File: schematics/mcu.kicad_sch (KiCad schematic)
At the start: 7 parts, among them SW0 SW_SPST, U1 ESP32-C3-WROOM-02

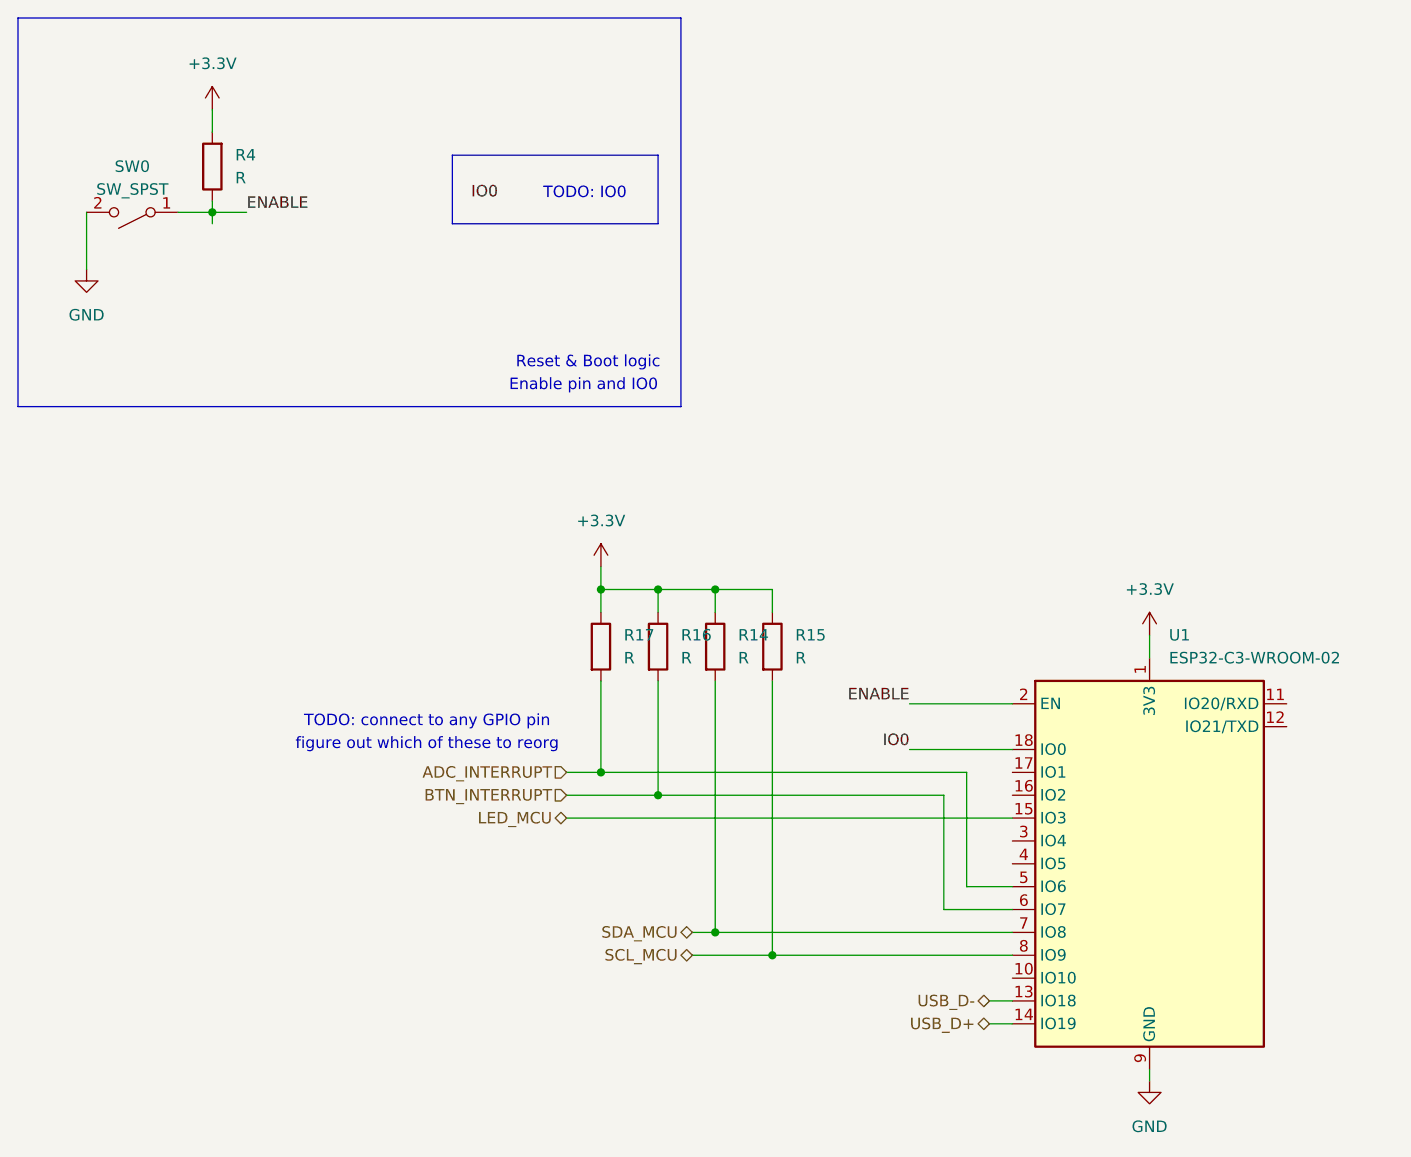
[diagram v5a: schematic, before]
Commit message: Fix layout, rewiring, and clearances
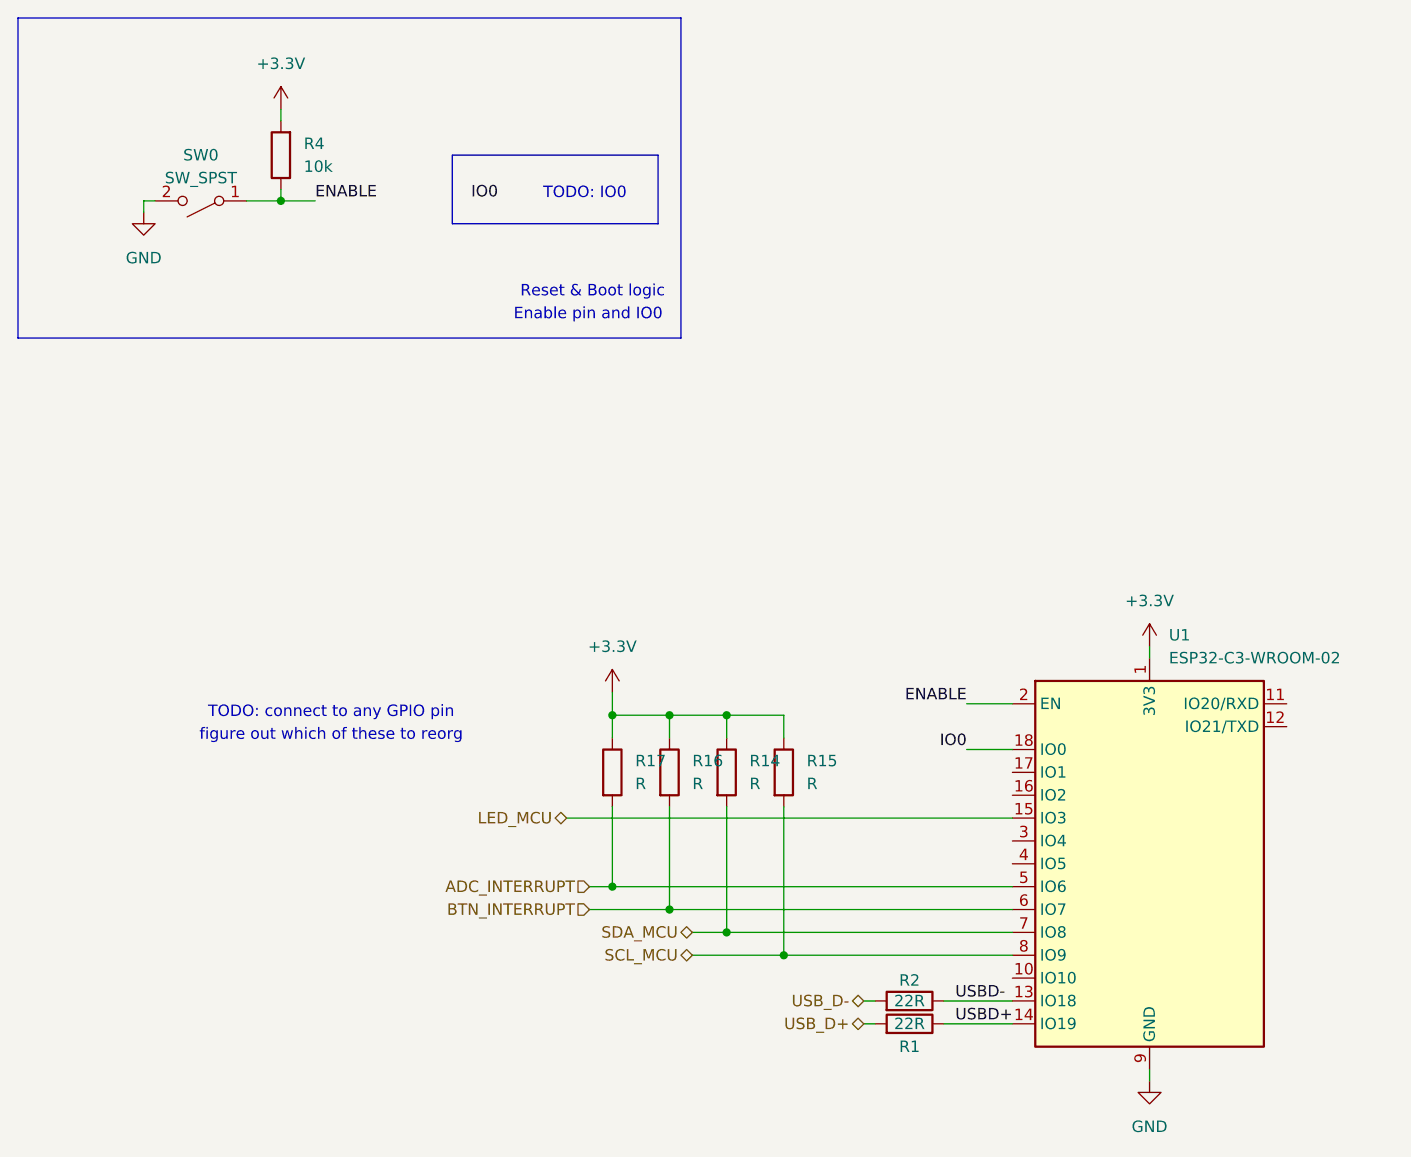
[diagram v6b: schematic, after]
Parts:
- added R1, R2: 22R, Resistor_SMD:R_0603_1608Metric, symbol Device:R
- R4: value R -> 10k
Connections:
- net USB_D+: now also R1.2; no longer U1.14 (IO19)
- net USB_D-: now also R2.2; no longer U1.13 (IO18)
- new net USBD+: R1.1, U1.14 (IO19)
- new net USBD-: R2.1, U1.13 (IO18)
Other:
- moved on the sheet: R14, R15, R16, R17, R4, SW0
